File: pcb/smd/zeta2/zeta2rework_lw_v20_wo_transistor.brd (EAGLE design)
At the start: 81 x 45.7 mm, 97 parts, among them IC1 MAX6520, U1 74HCT00D,652, U2 74HCT00D,652, U5 DS18B20U+

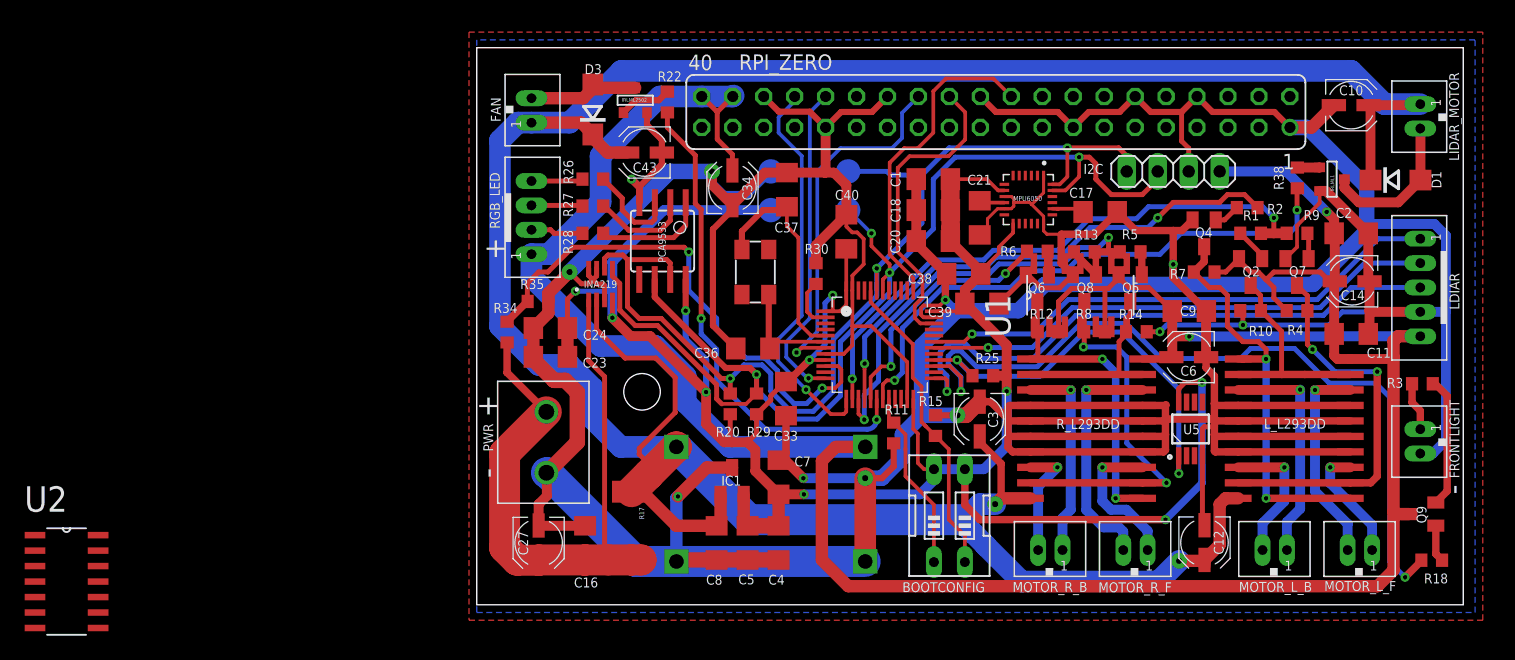
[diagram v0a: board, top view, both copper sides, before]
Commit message: removed l293d transistors
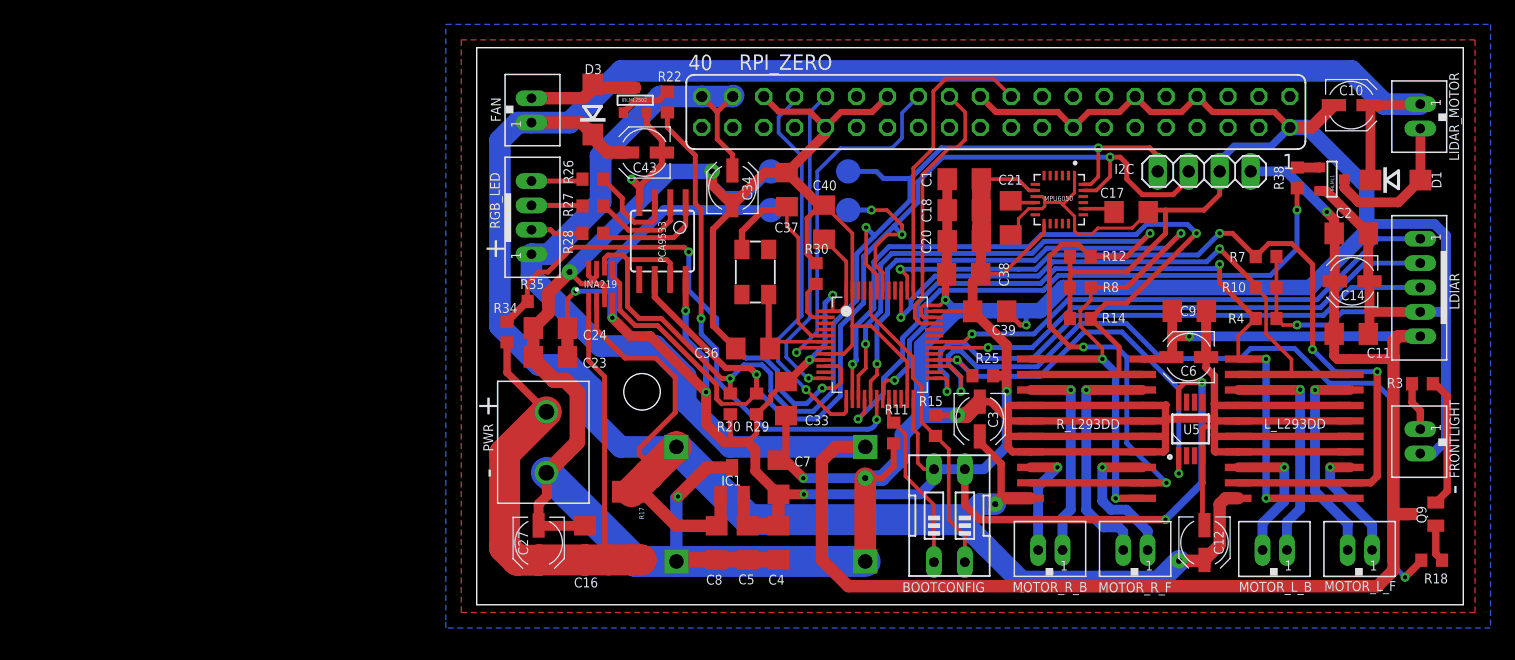
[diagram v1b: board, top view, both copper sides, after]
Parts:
- removed Q2, Q4, Q5, Q6, Q7, Q8: (no value), semicon-smd-ipc:SOT23
- removed R1, R13, R2, R5, R6, R9: 500R, rcl:R0603
- removed U1, U2: 74HCT00D,652, 74HCT00D_652:SOIC127P600X175-14N
- moved R12 6.71 mm to (48.9, 35.6)
- moved R7 5.24 mm to (64.1, 35.6), turned to 180 degrees
- moved R14 4.73 mm to (48.9, 30.5), turned to 0 degrees
- moved R8 3.82 mm to (48.9, 33.0)
- moved R4 2.62 mm to (64.1, 30.5)
- moved C1 2.54 mm to (39.4, 41.9)
- moved C17 2.54 mm to (53.1, 39.2)
- moved C18 2.54 mm to (39.4, 39.4)
- moved C20 2.54 mm to (39.4, 36.8)
- moved C21 2.54 mm to (43.2, 38.7)
- moved I2C 2.54 mm to (59.1, 42.5)
- moved MPU6050 2.54 mm to (47.2, 40.2)
- moved R10 2.29 mm to (64.1, 33.0), turned to 180 degrees
- moved C40 1.99 mm to (27.9, 38.4)
- moved C39 0.90 mm to (41.5, 31.1)
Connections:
- removed net EN1_EN2: U2.11, U2.12, U2.13, U2.8
- removed net IN1_IN4: U2.3, U2.4, U2.5
- removed net IN2_IN3: U2.6
- removed net M_DIR_1: R1.1, R9.1, STM32F103CB.14, U2.1, U2.2
- removed net M_DIR_2: R13.1, R5.1, STM32F103CB.15
- removed net N$1: L_L293DD.12, L_L293DD.9, Q7.3, R4.1
- removed net N$10: Q2.1, R1.2
- removed net N$11: Q4.1, R2.2
- removed net N$12: Q7.1, R9.2
- removed net N$13: Q5.1, R5.2
- removed net N$14: Q6.1, R6.2
- removed net N$15: Q8.1, R13.2
- removed net N$5: L_L293DD.19, L_L293DD.2, Q2.3, R10.2
- removed net N$6: Q8.3, R8.1, R_L293DD.12, R_L293DD.9
- removed net N$7: Q5.3, R14.2, R_L293DD.19, R_L293DD.2
- removed net N$8: L_L293DD.1, L_L293DD.11, Q4.3, R7.1
- removed net N$9: Q6.3, R12.1, R_L293DD.1, R_L293DD.11
- removed net PWM_M_EN_1: R2.1, STM32F103CB.16, U2.10, U2.9
- removed net PWM_M_EN_2: R6.1, STM32F103CB.17
- removed net VCC: U1.14
- new net M_DIR_L_1: L_L293DD.19, L_L293DD.2, R10.2, STM32F103CB.39
- new net M_DIR_L_2: L_L293DD.12, L_L293DD.9, R7.2, STM32F103CB.38
- new net M_DIR_R_1: R14.2, R_L293DD.19, R_L293DD.2, STM32F103CB.14
- new net M_DIR_R_2: R12.2, R_L293DD.12, R_L293DD.9, STM32F103CB.15
- new net PWM_M_EN_L: L_L293DD.1, L_L293DD.11, R4.2, STM32F103CB.16
- new net PWM_M_EN_R: R8.2, R_L293DD.1, R_L293DD.11, STM32F103CB.17
- net +5V: no longer Q2.2, Q5.2, R12.2, R4.2, R7.2, R8.2, U2.14
- net GND: now also R12.1, R4.1, R7.1, R8.1; no longer Q4.2, Q6.2, Q7.2, Q8.2, U1.7, U2.7
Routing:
- net M_DIR_R_2: track 0.00 -> 80.8 mm, vias 0 -> 4
- net PWM_M_EN_R: track 0.00 -> 72.7 mm, vias 0 -> 4
- net M_DIR_L_2: track 0.00 -> 72.2 mm, vias 0 -> 4
- net PWM_M_EN_L: track 0.00 -> 70.6 mm, vias 0 -> 4
- net M_DIR_R_1: track 0.00 -> 66.4 mm, vias 0 -> 2
- net M_DIR_L_1: track 0.00 -> 53.1 mm, vias 0 -> 2
- net M_DIR_1: track 47.7 -> 0.00 mm, vias 2 -> 0
- net PWM_M_EN_1: track 42.6 -> 0.00 mm, vias 2 -> 0
- net N$8: track 35.2 -> 0.00 mm, vias 2 -> 0
- net M_DIR_2: track 34.9 -> 0.00 mm, vias 2 -> 0
- net +5V: track 239.1 -> 204.4 mm
- net N$1: track 32.1 -> 0.00 mm, vias 2 -> 0
- net N$6: track 30.5 -> 0.00 mm, vias 2 -> 0
- net N$9: track 24.7 -> 0.00 mm, vias 2 -> 0
- net PWM_M_EN_2: track 20.7 -> 0.00 mm, vias 2 -> 0
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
